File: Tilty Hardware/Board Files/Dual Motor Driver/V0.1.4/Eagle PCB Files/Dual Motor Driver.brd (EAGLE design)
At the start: 38.4 x 50.8 mm, 42 parts, among them J1 AVR_SPI_PRG_62X3_LOCK, Q1 16MHz, U1 ATMEGA328P, U2 L298_BRIDGE_DRIVER, U3 LM2931

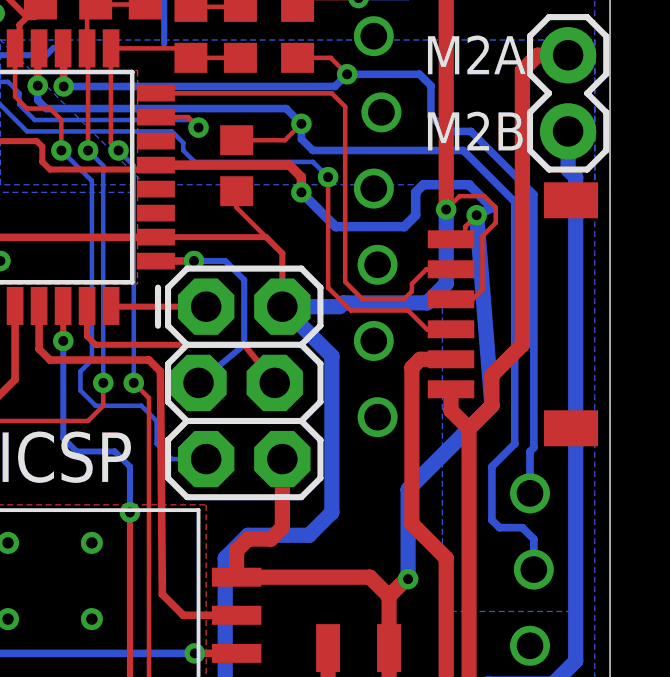
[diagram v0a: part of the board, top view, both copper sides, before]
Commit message: Added rudimentary speed control to Dual Motor Driver
Uses encoder ticks between updates and linearly adds or subtracts power
based on whether motor is faster or slower than it should be
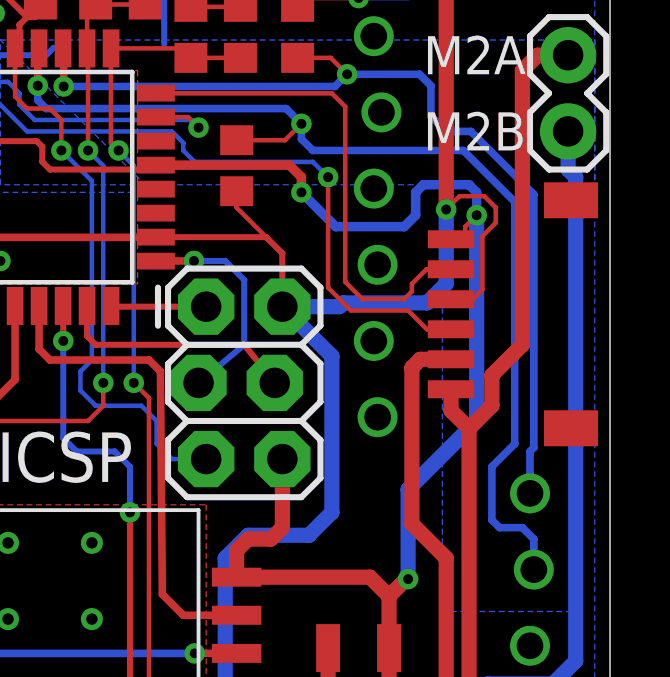
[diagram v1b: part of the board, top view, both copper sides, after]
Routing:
- net GND: track 257.5 -> 256.8 mm
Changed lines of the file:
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@@
 <wire x1="31.623" y1="26.2255" x2="31.623" y2="26.289" width="0.508" layer="1"/>
 <wire x1="31.623" y1="26.289" x2="30.988" y2="25.654" width="0.508" layer="1"/>
-<wire x1="33.909" y1="38.354" x2="34.417" y2="32.004" width="0.508" layer="16"/>
-<wire x1="34.417" y1="32.004" x2="31.623" y2="29.21" width="0.508" layer="16"/>
+<wire x1="33.909" y1="38.354" x2="33.909" y2="31.496" width="0.508" layer="16"/>
+<wire x1="33.909" y1="31.496" x2="31.623" y2="29.21" width="0.508" layer="16"/>
 <wire x1="31.623" y1="29.21" x2="31.623" y2="26.2255" width="0.508" layer="16"/>
 <wire x1="23.2156" y1="40.024" x2="22.879" y2="40.024" width="0.2032" layer="1"/>
@@
 <wire x1="31.877" y1="39.116" x2="32.131" y2="39.37" width="0.3175" layer="16"/>
 <wire x1="32.131" y1="39.37" x2="33.655" y2="39.37" width="0.3175" layer="16"/>
-<wire x1="33.655" y1="39.37" x2="34.417" y2="38.608" width="0.3175" layer="16"/>
-<wire x1="34.417" y1="38.608" x2="33.909" y2="38.354" width="0.3175" layer="16"/>
+<wire x1="33.655" y1="39.37" x2="33.909" y2="39.116" width="0.3175" layer="16"/>
+<wire x1="33.909" y1="39.116" x2="33.909" y2="38.354" width="0.3175" layer="16"/>
 <wire x1="23.2156" y1="40.024" x2="27.667" y2="40.024" width="0.3175" layer="1"/>
 <wire x1="27.667" y1="40.024" x2="28.067" y2="39.624" width="0.3175" layer="1"/>

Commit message: Updated Dual Motor Driver to (hopefully) final revision
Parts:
- removed S1: SWITCH-MOMENTARY-2SMD, SparkFun-Electromechanical:TACTILE_SWITCH_SMD
- JP8: device SparkFun-Connectors:1X04_LOCK -> SparkFun-Connectors:1X05
- moved JP8 1.02 mm to (24.3, 49.3)
- moved C2 0.51 mm to (11.0, 33.3)
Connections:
- net GND: no longer S1.1
- net RESET: now also JP8.5; no longer S1.3
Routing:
- net GND: track 256.8 -> 228.7 mm, vias 25 -> 24
- net RESET: track 28.3 -> 29.5 mm, vias 1 -> 2
- net RX: track 7.36 -> 6.29 mm
- net +5V: track 168.9 -> 169.9 mm
- net N$4: track 42.2 -> 42.8 mm
- added copper zone on layer 16, net N$3
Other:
- board text added: "RST"
- board text removed: "Reset"
